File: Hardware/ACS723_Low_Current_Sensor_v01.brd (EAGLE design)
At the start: 29.2 x 15.2 mm, 19 parts, among them U1 ACS712, U2 OPA344

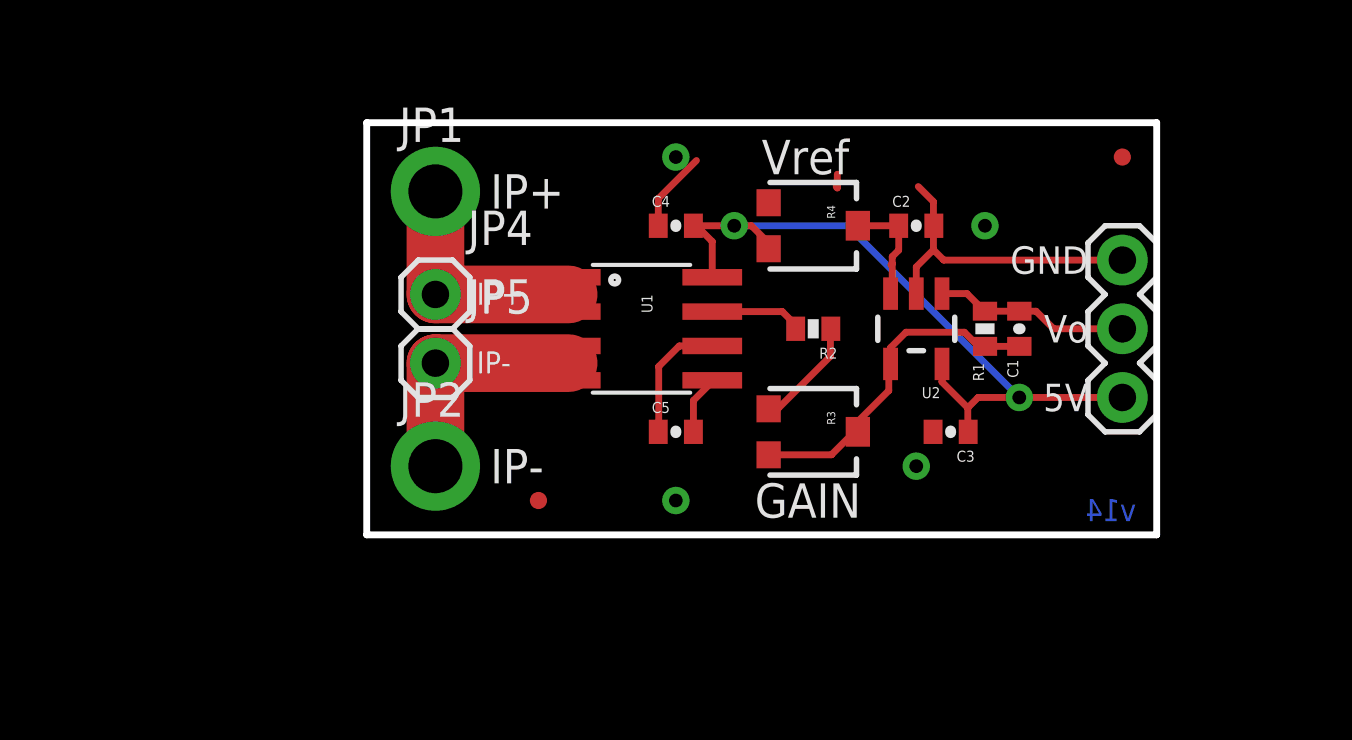
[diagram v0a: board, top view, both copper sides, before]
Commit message: Rerouting and deletion of original files
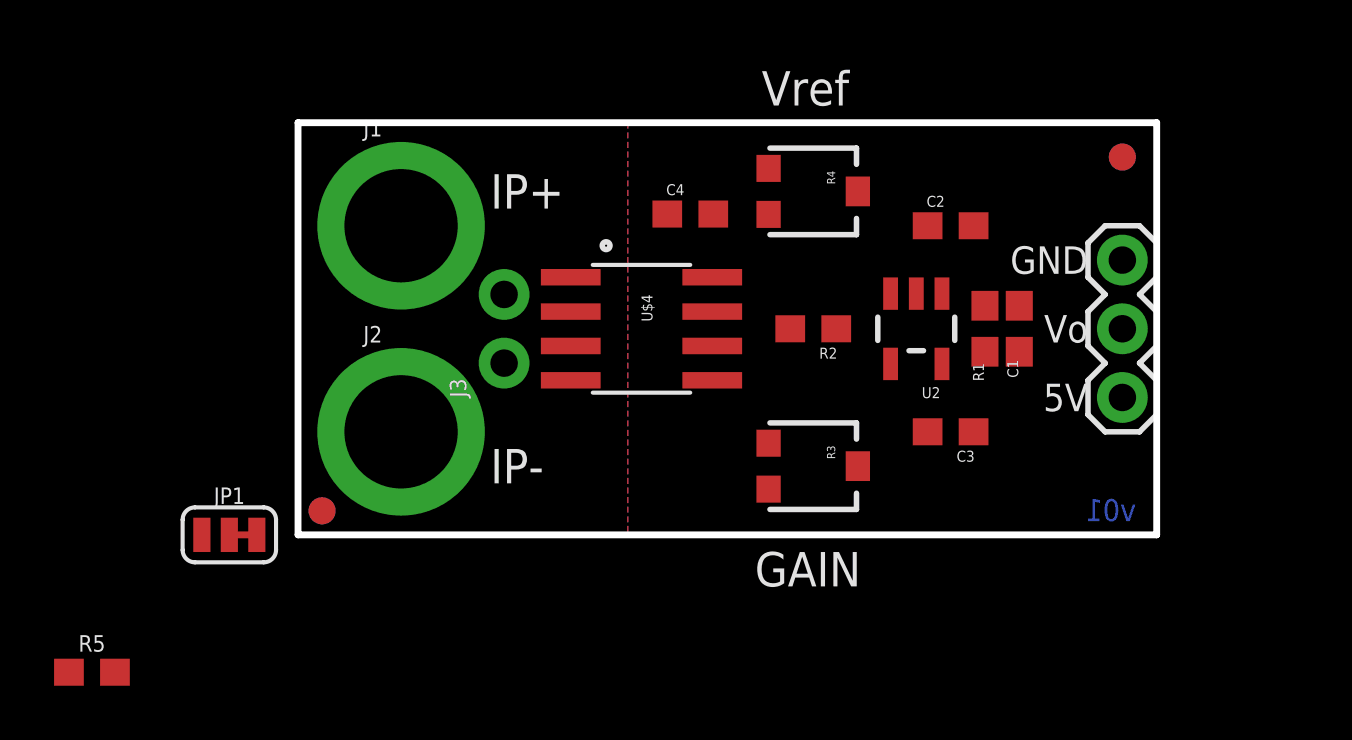
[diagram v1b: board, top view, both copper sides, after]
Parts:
- removed C5: 1nF, SparkFun:0402-CAP
- removed JP2: M01PTH_2MM, SparkFun:1X01_2MM
- removed JP4, JP5: M01PTH, SparkFun:1X01
- removed U$1, U$3: FIDUCIALUFIDUCIAL, SparkFun:MICRO-FIDUCIAL
- removed U1: ACS712, SparkFun:SO08
- added FD1, FD2, FD3, FD4: FIDUCIAL1X2, SparkFun-Aesthetics:FIDUCIAL-1X2
- added J1, J2: (no value), SparkFun-Connectors:SMTSO-256-ET-0.165DIA
- added J3: (no value), SparkFun-Connectors:1X02_NO_SILK
- added R5: 4.7k, SparkFun-Resistors:0603
- added U$4: ACS723, SparkFun-IC-Power:SO08
- C1, C2, C3, C4: device SparkFun:0402-CAP -> SparkFun-Capacitors:0603
- JP1: value M01PTH_2MM -> JUMPER-SMT_3_1-NC_TRACE_SILK; device SparkFun:1X01_2MM -> SparkFun-Jumpers:SMT-JUMPER_3_1-NC_TRACE_SILK
- R1: value 47K -> 47k; device SparkFun:0402-RES -> SparkFun-Resistors:0603
- R2: value 1K -> 1k; device SparkFun:0402-RES -> SparkFun-Resistors:0603
- moved JP1 14.8 mm to (-5.08, 0.00)
- moved R3 1.27 mm to (16.5, 2.54)
- moved C2 1.27 mm to (21.6, 11.4)
- moved R4 1.27 mm to (16.5, 12.7)
- moved C4 0.69 mm to (12.0, 11.9)
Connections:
- removed net N$8: C5.1, U1.6
- new net BW_SEL: JP1.2, U$4.6
- new net N$1: JP1.3, R5.1
- net 5V: now also R5.2, U$4.5, U$4.8; no longer U1.8
- net GND: now also JP1.1; no longer C5.2, U1.5
- net IP+: now also J1.P$1, J3.2, U$4.1, U$4.2; no longer JP1.1, JP4.1, U1.1, U1.2
- net IP-: now also J2.P$1, J3.1, U$4.3, U$4.4; no longer JP2.1, JP5.1, U1.3, U1.4
- net N$3: now also U$4.7; no longer U1.7
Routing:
- net 5V: track 27.8 -> 0.00 mm, vias 2 -> 0
- net GND: track 17.4 -> 0.00 mm, vias 4 -> 0
- net N$5: track 12.7 -> 0.00 mm
- net IP-: track 10.2 -> 0.00 mm
- net IP+: track 10.2 -> 0.00 mm
- net VO: track 7.24 -> 0.00 mm
- net N$8: track 4.72 -> 0.00 mm
- net N$4: track 4.37 -> 0.00 mm
- net N$6: track 4.31 -> 0.00 mm
- net N$3: track 3.63 -> 0.00 mm
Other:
- board size 29.2 x 15.2 mm -> 31.8 x 15.2 mm
- board text added: "v01"
- board text removed: "v14"

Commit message: Finalizing v01
-reduced GND plane to isolate from IP pins
-swapped all existing 0402 packages to 0603
-updated trimpot packages
-added extra copper for large IP traces on bottom copper
-added bandwidth select jumper
-swapped in new opamp symbol and package
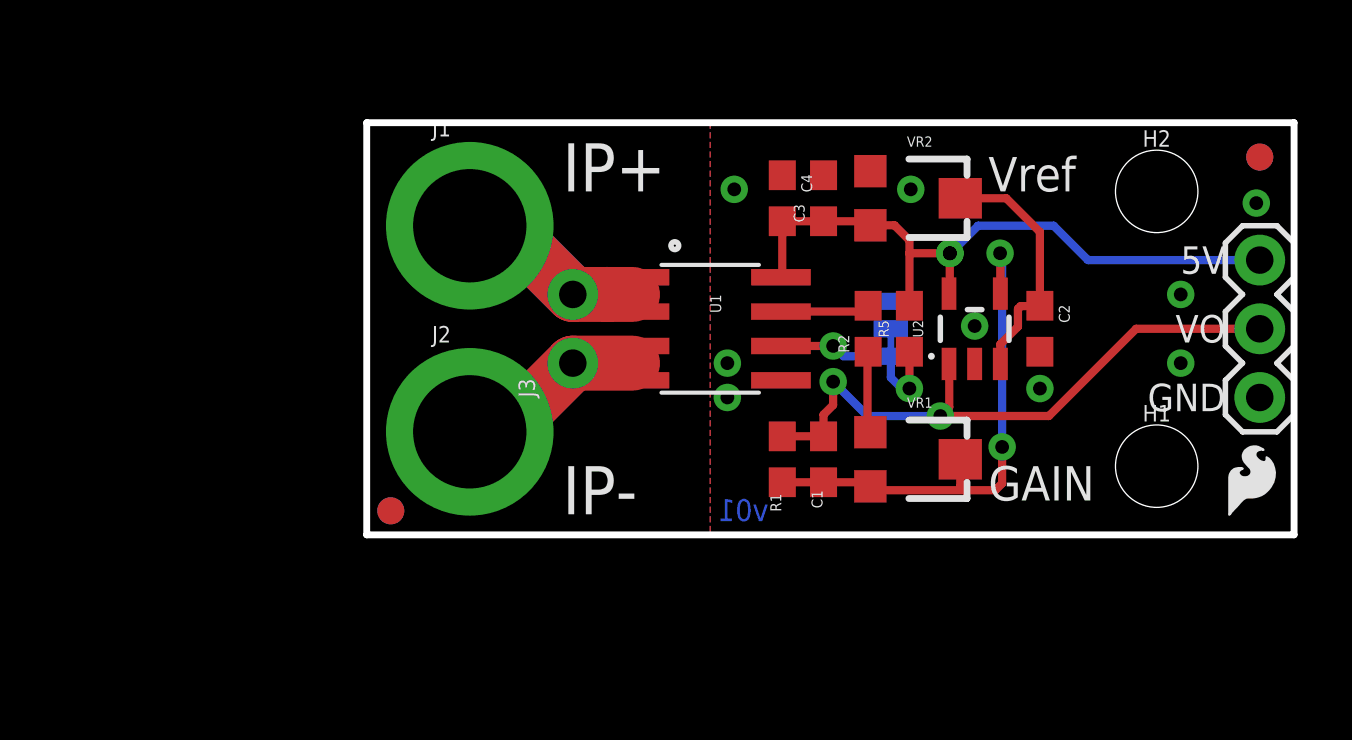
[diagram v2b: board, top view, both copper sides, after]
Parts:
- removed R3, R4: TRIMPOTSMD, SparkFun:TRIMPOT-3MM
- removed U$2: LOGO-SFENEW, SparkFun:SFE-NEW-WEBLOGO
- removed U$4: ACS723, SparkFun-IC-Power:SO08
- added FRAME1: FRAME-LETTER, SparkFun-Aesthetics:CREATIVE_COMMONS
- added H1, H2: STAND-OFFTIGHT, SparkFun-Hardware:STAND-OFF-TIGHT
- added LOGO1: SFE_LOGO_NAME_FLAME.1_INCH, SparkFun-Aesthetics:SFE_LOGO_NAME_FLAME_.1
- added LOGO2: OSHW-LOGOS, SparkFun-Aesthetics:OSHW-LOGO-S
- added LOGO3: SFE_LOGO_FLAME.1_INCH, SparkFun-Aesthetics:SFE_LOGO_FLAME_.1
- added U1: ACS723ACS723LLCTR-05AB-T2, SparkFun-IC-Power:SO08
- added VR1, VR2: 10k, SparkFun-Resistors:TRIMPOT-SMD-TC33X
- U2: device SparkFun:SOT23-5 -> SparkFun-IC-Amplifiers:SOT23-5
- moved R5 32.8 mm to (20.1, 7.62), turned to 90 degrees
- moved JP1 25.6 mm to (19.4, 7.62), flipped to the bottom, turned to 270 degrees
- moved C3 9.83 mm to (16.9, 12.4), turned to 90 degrees
- moved R1 8.91 mm to (15.4, 2.79)
- moved C1 8.70 mm to (16.9, 2.79)
- moved JP3 7.18 mm to (33.0, 10.2), turned to 270 degrees
- moved FD3 5.08 mm to (33.0, 14.0)
- moved FD4 5.08 mm to (33.0, 14.0)
- moved C2 5.04 mm to (24.9, 7.62), turned to 270 degrees
- moved C4 3.45 mm to (15.4, 12.4), turned to 270 degrees
- moved FD1 2.54 mm to (0.89, 0.89)
- moved FD2 2.54 mm to (0.89, 0.89)
- moved J1 2.54 mm to (3.81, 11.4)
- moved J2 2.54 mm to (3.81, 3.81)
- moved J3 2.54 mm to (7.62, 6.35)
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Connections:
- net 5V: now also U1.8, VR2.3; no longer R4.3, U$4.5, U$4.8
- net BW_SEL: now also U1.6; no longer U$4.6
- net GND: now also U1.5, VR2.1; no longer R4.1
- net IP+: now also U1.1, U1.2; no longer U$4.1, U$4.2
- net IP-: now also U1.3, U1.4; no longer U$4.3, U$4.4
- net N$3: now also U1.7; no longer U$4.7
- net N$4: now also VR1.1; no longer R3.1
- net N$5: now also VR1.2, VR1.3; no longer R3.2, R3.3
- net N$6: now also VR2.2; no longer R4.2
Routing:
- net 5V: track 0.00 -> 24.9 mm, vias 0 -> 2
- net VO: track 0.00 -> 23.4 mm, vias 0 -> 2
- net N$5: track 0.00 -> 19.5 mm, vias 0 -> 2
- net IP+: track 0.00 -> 14.1 mm
- net IP-: track 0.00 -> 13.4 mm
- net N$6: track 0.00 -> 9.36 mm
- net BW_SEL: track 0.00 -> 4.22 mm, vias 0 -> 1
- net N$3: track 0.00 -> 3.31 mm
- net N$4: track 0.00 -> 3.03 mm
- net N$1: track 0.00 -> 3.00 mm, vias 0 -> 1
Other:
- board size 31.8 x 15.2 mm -> 34.3 x 15.2 mm
- board text added: "20kHz"
- board text added: "80kHz"
- board text added: "ACS723 Low Current Sensor"
- board text added: "VO"
- board text removed: "ACS712 Low Current"
- board text removed: "Sensor Board v1"
- board text removed: "Vo"

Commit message: Silk and designer details
-added "designed by" and "revised by" attributes in the SCH and BRD
-adjusted silk
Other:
- board text added: "Eric Orosel"
- board text added: "Pete Dokter"
- board text added: "Revised by:"
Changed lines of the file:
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@@
 <layer number="47" name="Measures" color="7" fill="1" visible="no" active="yes"/>
 <layer number="48" name="Document" color="7" fill="1" visible="no" active="yes"/>
-<layer number="49" name="Reference" color="13" fill="1" visible="no" active="yes"/>
+<layer number="49" name="Reference" color="13" fill="1" visible="yes" active="yes"/>
 <layer number="50" name="dxf" color="7" fill="1" visible="no" active="yes"/>
 <layer number="51" name="tDocu" color="6" fill="1" visible="yes" active="yes"/>
@@
 <text x="7.239" y="12.7" size="1.778" layer="21" ratio="15">IP+</text>
 <text x="7.239" y="0.762" size="1.778" layer="21" ratio="15">IP-</text>
-<text x="25.4" y="9.779" size="1.143" layer="22" ratio="15" rot="MR0">ACS723
+<text x="25.908" y="10.033" size="1.143" layer="22" ratio="15" rot="MR0">ACS723
 Low Current
 Sensor</text>
@@
 <text x="7.3914" y="10.16" size="1.27" layer="22" ratio="15" rot="MR90">IP+</text>
 <text x="7.3914" y="2.2098" size="1.27" layer="22" ratio="15" rot="MR90">IP-</text>
+<text x="17.78" y="-12.7" size="2.032" layer="51" font="vector" ratio="7">Pete Dokter</text>
+<text x="-1.524" y="-15.24" size="2.032" layer="51" font="vector" ratio="7">Revised by:</text>
+<text x="18.288" y="-15.24" size="2.032" layer="51" font="vector" ratio="7">Eric Orosel</text>
 </plain>
 <attributes>

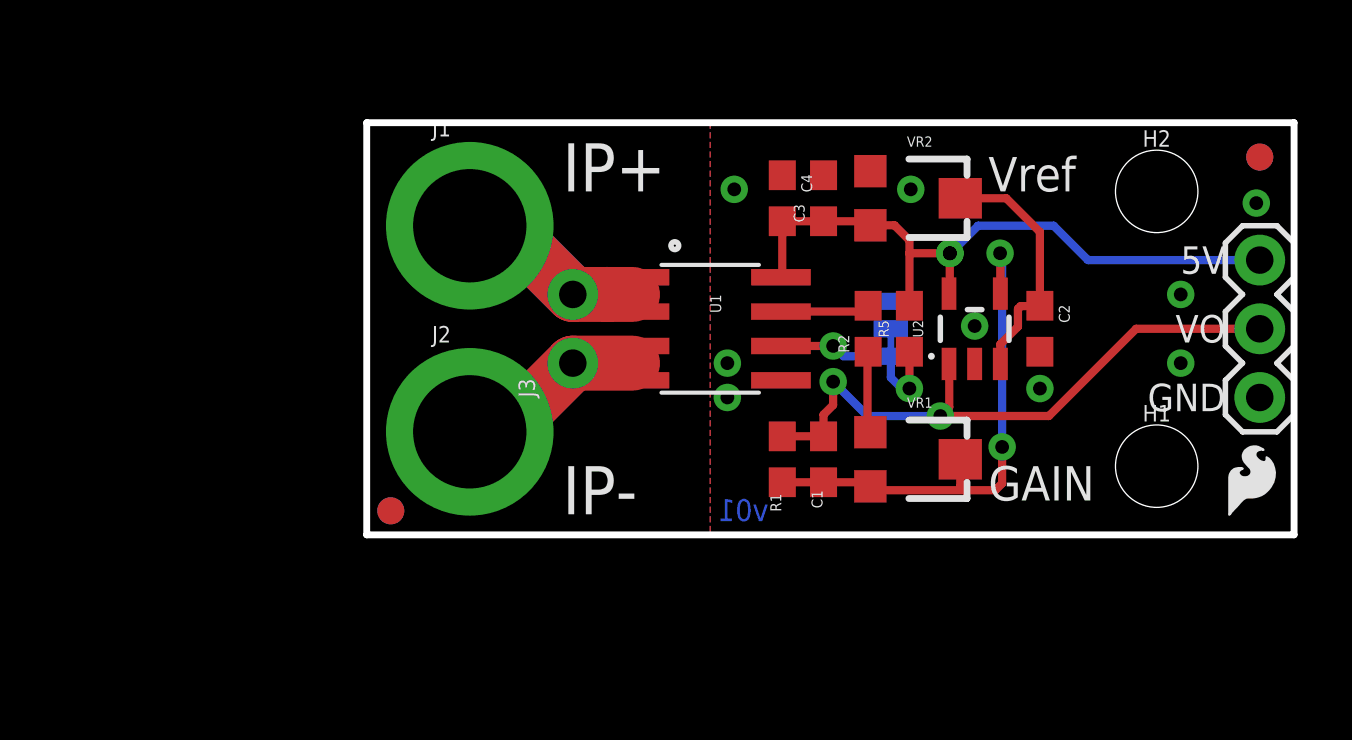
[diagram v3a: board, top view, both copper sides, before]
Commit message: finalize for checklist
-removed oen standoff
-added 1nf cap
-moved silk
-moved header for output
-added measures
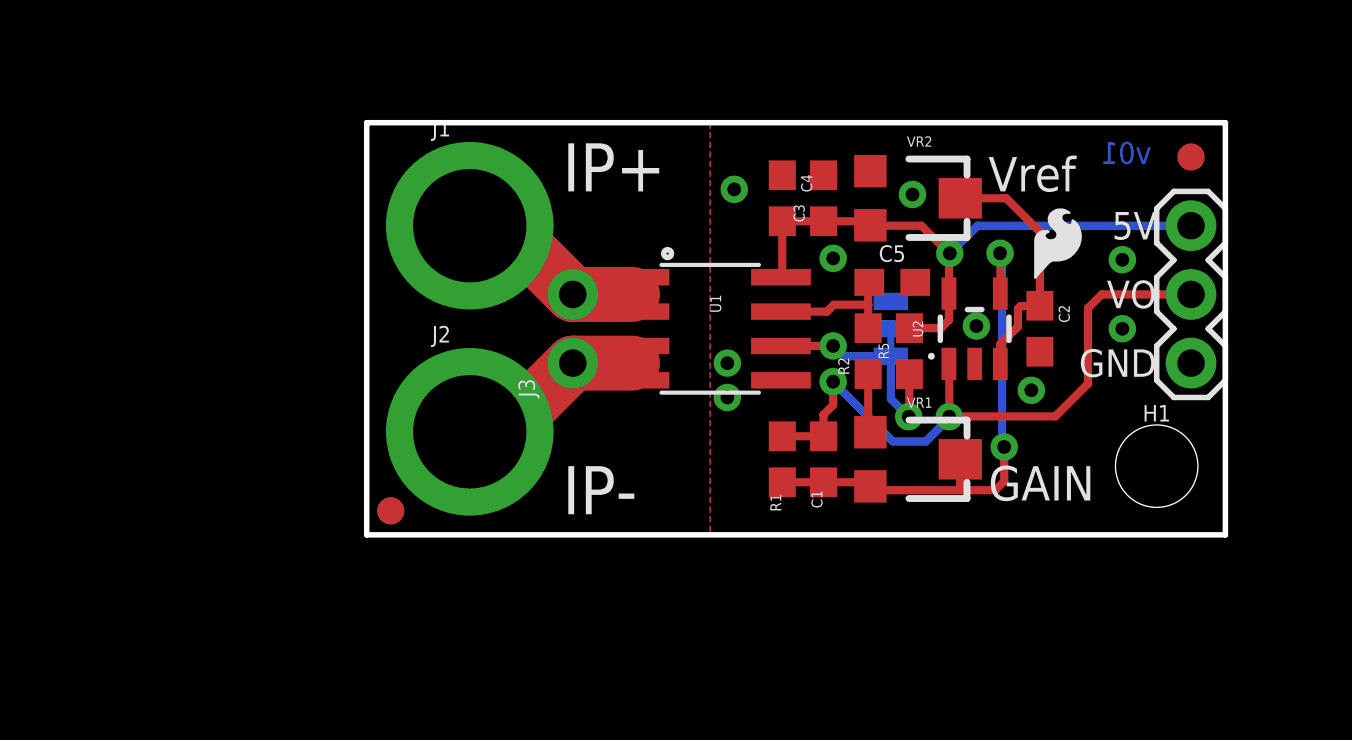
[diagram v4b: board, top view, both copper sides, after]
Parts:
- removed H2: STAND-OFFTIGHT, SparkFun-Hardware:STAND-OFF-TIGHT
- added C5: 1nF, SparkFun-Capacitors:0603
- U1: value ACS723ACS723LLCTR-05AB-T2 -> ACS723; device SparkFun-IC-Power:SO08 -> SparkFun-Sensors:SO08
- moved LOGO2 12.2 mm to (15.2, 9.59)
- moved LOGO3 11.3 mm to (24.4, 9.14)
- moved LOGO1 3.69 mm to (22.7, 0.51)
- moved JP3 2.84 mm to (30.5, 11.4)
- moved FD3 2.54 mm to (30.5, 14.0)
- moved FD4 2.54 mm to (30.5, 14.0)
- moved R2 0.83 mm to (18.5, 6.79)
- moved R5 0.83 mm to (20.1, 6.79)
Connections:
- removed net N$3: R2.2, U1.7
- new net VIOUT: C5.1, R2.2, U1.7
- net GND: now also C5.2
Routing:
- net VIOUT: track 0.00 -> 4.98 mm
- net N$3: track 3.31 -> 0.00 mm
- net 5V: track 24.9 -> 22.2 mm, vias 2 -> 1
- net N$1: track 3.00 -> 4.09 mm
- net N$4: track 3.03 -> 2.18 mm
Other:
- board size 34.3 x 15.2 mm -> 31.8 x 15.2 mm
- board text added: "ACS723 Low Current"
- board text added: "Sensor"
- board text removed: "ACS723 Low Current Sensor"

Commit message: Changes per v01 checklist
-moved R1 and C1 closer to the opamp
-moved silk
-moved fiducials
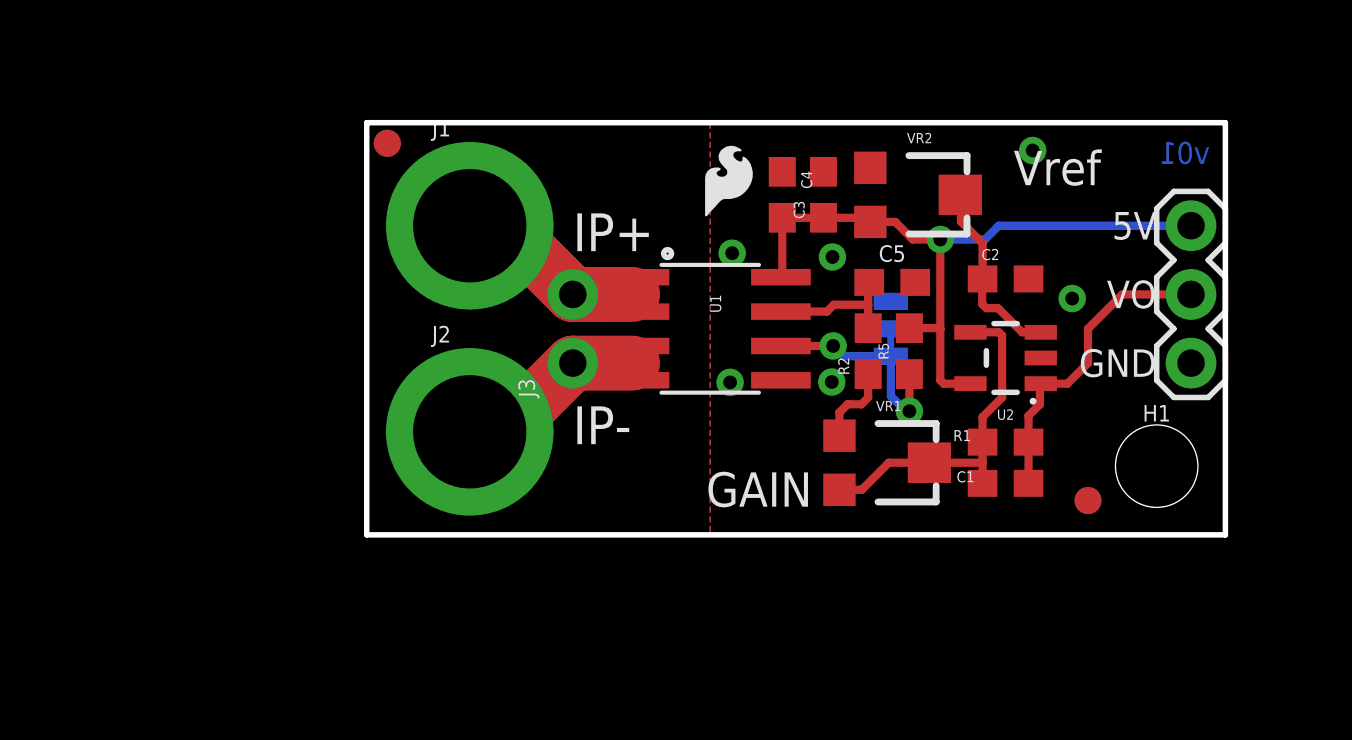
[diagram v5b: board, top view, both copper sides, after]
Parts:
- moved FD1 13.6 mm to (0.76, 14.5)
- moved FD2 13.6 mm to (0.76, 14.5)
- moved FD3 13.3 mm to (26.7, 1.27)
- moved FD4 13.3 mm to (26.7, 1.27)
- moved LOGO3 12.4 mm to (12.2, 11.5)
- moved R1 8.28 mm to (23.6, 3.43), turned to 180 degrees
- moved LOGO2 7.98 mm to (12.2, 2.20)
- moved C1 6.79 mm to (23.6, 1.91), turned to 180 degrees
- moved LOGO1 3.29 mm to (26.0, 0.18)
- moved C2 2.24 mm to (23.6, 9.46), turned to 0 degrees
- moved U2 1.57 mm to (23.6, 6.54), turned to 90 degrees
- moved VR1 1.15 mm to (19.3, 2.67)
- moved C3 0.13 mm to (16.9, 12.6)
- moved C4 0.13 mm to (15.4, 12.6)
- moved VR2 0.13 mm to (20.4, 12.6)
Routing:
- net VO: track 23.8 -> 11.5 mm, vias 2 -> 0
- net N$5: track 19.7 -> 12.7 mm, vias 2 -> 0
- net 5V: track 22.2 -> 25.7 mm
- net N$6: track 9.36 -> 6.98 mm
- net N$4: track 2.18 -> 3.02 mm
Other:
- board text added: "ACS723"
- board text added: "Low Current Sensor"
- board text removed: "ACS723 Low Current"
- board text removed: "Sensor"
